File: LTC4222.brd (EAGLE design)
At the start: 160 x 100 mm, 24 parts

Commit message: Forgot to save the first time
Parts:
- added U$3, U$4: 74HC1G86GW-Q100H, Baja_Parts_Lib:SOT65P212X110-5M
- added U$5: SN74HC74QPWRQ1, Baja_Parts_Lib:SOP65P640X120-14M
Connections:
- new net N$1: U$3.2, U$3.4, U$5.2
- new net N$2: U$4.2, U$4.4, U$5.12
- new net N$3: U$12.17, U$5.9
- new net N$4: U$12.24, U$5.5
- net GND: now also U$3.3, U$4.3, U$5.7

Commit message: LTC4222 Schematic Design V2
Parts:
- removed U$1, U$2: TNPW060310K0BEEN, Baja_Parts_Lib:AT0603
- removed U$12: LTC4222, Baja_Parts_Lib:QFN50P500X500X75-33T345M
- removed U$13: AT0603DRD071K82L, Baja_Parts_Lib:RESC1608X45M
- removed U$14: TNPW0603392RBEEA, Baja_Parts_Lib:AT0603
- removed U$15: TNPW0603953RBEEA, Baja_Parts_Lib:AT0603
- removed U$16: CGA3E1X7R1V105K080AE, Baja_Parts_Lib:CAPC1608X80M
- removed U$17: CGA2B3X7R1E683K050BB, Baja_Parts_Lib:CAPC1005X50M
- removed U$18: CGA3E2X7R1H104K080AE, Baja_Parts_Lib:CAPC1608X80M
- removed U$19, U$30: WSL0603R0180FEA, Baja_Parts_Lib:RESC1507X40M
- removed U$20, U$31: PMV15ENEAR, Baja_Parts_Lib:SOT95P230X110-3M
- removed U$21, U$32: TNPW060310R0BEEN, Baja_Parts_Lib:AT0603
- removed U$22: 67997-100HLF, Baja_Parts_Lib:HDRV2W64P254_2X1_241X508X838B
- removed U$23: CGA2B3X7R1V223K050BB, Baja_Parts_Lib:CAPC1005X50M
- removed U$24, U$33: MCT0603PD4991DP500, Baja_Parts_Lib:RESC1508X47M
- removed U$25, U$34: TNPW06033K57BEEA, Baja_Parts_Lib:AT0603
- removed U$27: TNPW060334K0BEEA, Baja_Parts_Lib:AT0603
- removed U$28: TNPW06031K02BEEA, Baja_Parts_Lib:AT0603
- removed U$29: AT0603DRD073K4L, Baja_Parts_Lib:RESC1608X45M
- added C1, C2, C5: CGA3E2X7R1H104K080AE, Baja_Parts_Lib:CAPC1608X80M
- added C3: CGA3E1X7R1V105K080AE, Baja_Parts_Lib:CAPC1608X80M
- added C4: CGA2B3X7R1E683K050BB, Baja_Parts_Lib:CAPC1005X50M
- added C6: CGA2B3X7R1V223K050BB, Baja_Parts_Lib:CAPC1005X50M
- added IC1: 67997-100HLF, Baja_Parts_Lib:HDRV2W64P254_2X1_241X508X838B
- added IC2: LTC4222, Baja_Parts_Lib:QFN50P500X500X75-33T345M
- added J1, J2: PMV15ENEAR, Baja_Parts_Lib:SOT95P230X110-3M
- added R1, R12: WSL0603R0180FEA, Baja_Parts_Lib:RESC1507X40M
- added R10: TNPW0603392RBEEA, Baja_Parts_Lib:AT0603
- added R11: TNPW0603953RBEEA, Baja_Parts_Lib:AT0603
- added R13, R5: TNPW060310R0BEEN, Baja_Parts_Lib:AT0603
- added R14, R8: TNPW060310K0BEEN, Baja_Parts_Lib:AT0603
- added R15, R7: TNPW06033K57BEEA, Baja_Parts_Lib:AT0603
- added R16: MCT0603PD4991DP500, Baja_Parts_Lib:RESC1508X47M
- added R2: TNPW060334K0BEEA, Baja_Parts_Lib:AT0603
- added R3: TNPW06031K02BEEA, Baja_Parts_Lib:AT0603
- added R4: AT0603DRD073K4L, Baja_Parts_Lib:RESC1608X45M
- added R6: TNPW040210K2BEED, Baja_Parts_Lib:RESC1005X35M
- added R9: AT0603DRD071K82L, Baja_Parts_Lib:RESC1608X45M
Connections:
- removed net N$29: U$12.2, U$12.3, U$12.7, U$18.2
- removed net N$30: U$12.11, U$13.1, U$19.2
- removed net N$31: U$20.1, U$21.1, U$22.1
- removed net N$32: U$12.13, U$21.2
- removed net N$33: U$22.2, U$23.2
- removed net N$34: U$12.14, U$2.1, U$20.2, U$23.1, U$24.1
- removed net N$35: U$12.15, U$24.2, U$25.1
- removed net N$36: U$12.32, U$28.2, U$29.1
- removed net N$37: U$12.16, U$2.2
- removed net N$38: U$12.31, U$27.2, U$28.1
- removed net N$39: U$12.30, U$27.1, U$30.1
- removed net N$40: U$12.29, U$30.2, U$31.2
- removed net N$41: U$31.1, U$32.1
- removed net N$42: U$12.28, U$32.2
- removed net N$43: U$1.1, U$12.27, U$31.3, U$33.1
- removed net N$44: U$1.2, U$12.25
- removed net N$45: U$12.26, U$33.2, U$34.1
- new net N$10: C2.2, IC2.2, IC2.3
- new net N$11: IC2.28, R5.1
- new net N$12: IC2.27, J1.2, R6.2, R8.2
- new net N$13: IC2.26, R6.1, R7.2
- new net N$14: IC2.25, R8.1
- new net N$15: C4.2, IC2.8
- new net N$16: C3.2, IC2.1
- new net N$17: C3.1, C4.1
- new net N$18: IC2.13, R13.2
- new net N$19: IC2.9, R10.2, R11.1
- new net N$20: IC2.12, J2.3, R12.2
- new net N$21: IC2.11, R12.1, R9.1
- new net N$22: IC1.1, J2.1, R13.1
- new net N$23: C6.2, IC2.14, J2.2, R14.1, R16.1
- new net N$5: U$4.4, U$5.12
- new net N$6: IC2.29, J1.3, R1.2
- new net N$7: IC2.32, R3.1, R4.1
- new net N$8: C1.2, IC2.31, R2.1, R3.2
- new net N$9: R5.2
- net GND: now also C1.1, C2.1, C5.1, IC2.4, R11.2, R4.2, R7.1; no longer U$12.4, U$15.2, U$16.1, U$17.1, U$18.1, U$25.2, U$29.2, U$34.2
- net N$1: no longer U$3.2
- net N$2: now also IC2.30, R1.1, R2.2; no longer U$4.2, U$4.4, U$5.12
- net N$24: now also C6.1, IC1.2; no longer U$12.10, U$13.2, U$14.1
- net N$25: now also IC2.15, R15.1, R16.2; no longer U$12.9, U$14.2, U$15.1
- net N$26: now also IC2.16, R14.2; no longer U$12.8, U$16.2
- net N$27: now also C5.2, IC2.10, R10.1, R9.2; no longer U$12.1, U$17.2
- net N$28: now also R15.2; no longer U$12.12, U$19.1, U$20.3
- net N$3: now also IC2.17, U$4.1; no longer U$12.17
- net N$4: now also IC2.24, U$3.2; no longer U$12.24

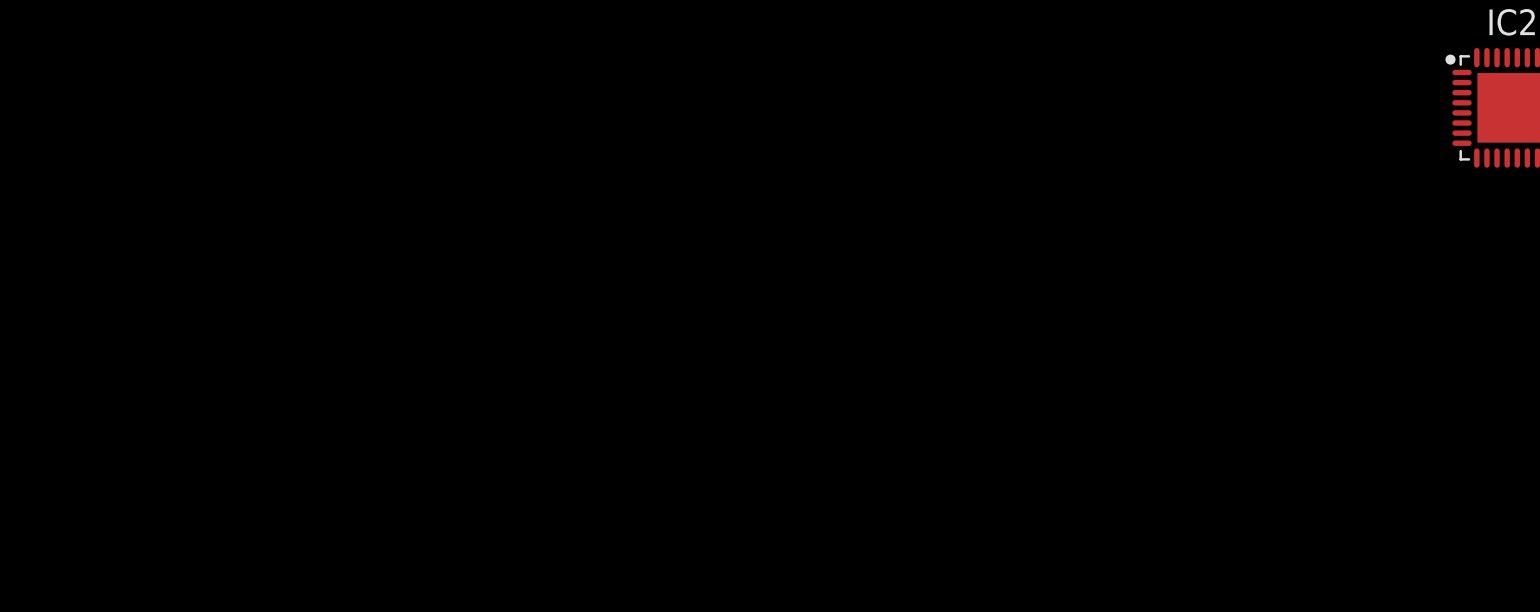
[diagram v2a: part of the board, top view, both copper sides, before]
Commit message: Polished LTC4222 schematic and added test points. Started on pin heads
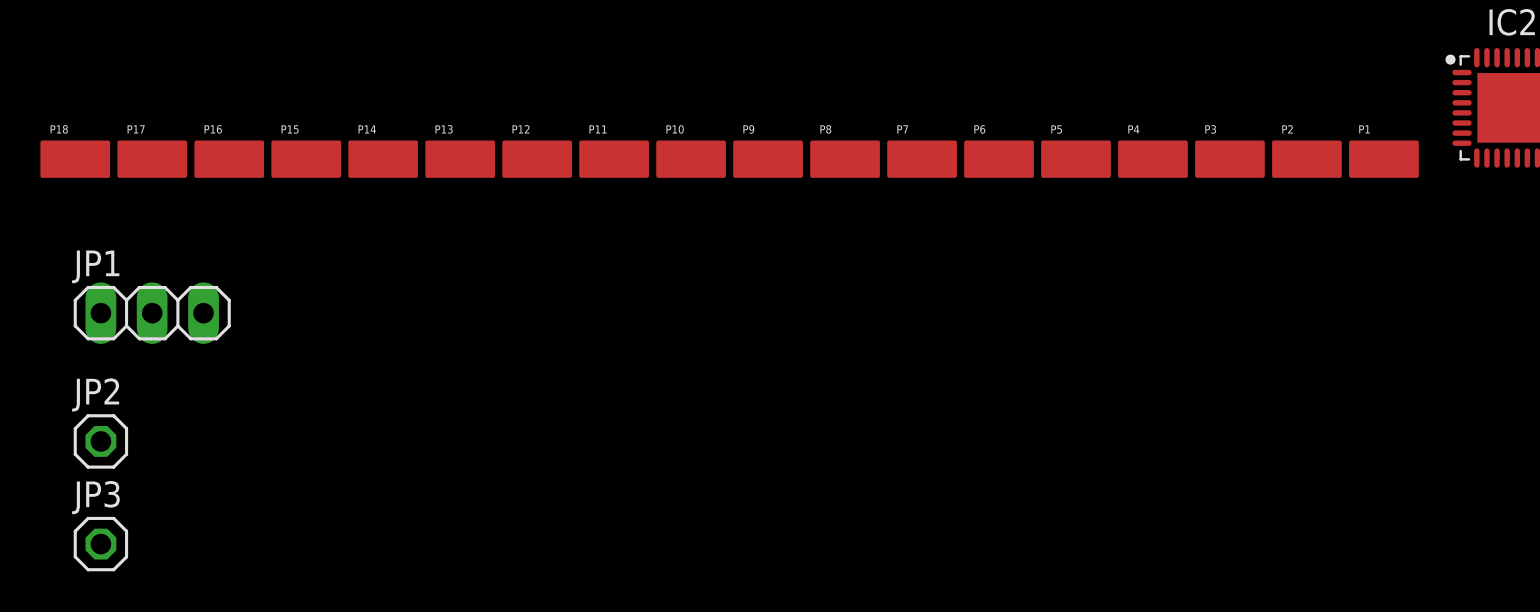
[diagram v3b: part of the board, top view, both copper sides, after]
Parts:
- added JP1: (no value), pinhead:1X03
- added JP2, JP3: (no value), pinhead:1X01
- added P1, P10, P11, P12, P13, P14, P15, P16, P17, P18, P2, P3, P4, P5, P6, P7, P8, P9: S1751-46R, Baja_Parts_Lib:S1751-46R
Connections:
- new net N$29: IC2.26, P7.1, R6.1, R7.2
- new net N$30: IC2.6, JP1.2
- new net N$31: IC2.5, JP1.3
- net N$11: now also P5.1
- net N$12: now also P6.1
- net N$13: now also IC2.7, JP1.1; no longer IC2.26, R6.1, R7.2
- net N$14: now also P8.1
- net N$18: now also P14.1
- net N$19: now also P18.1
- net N$2: now also JP2.1, P2.1
- net N$20: now also P15.1
- net N$21: now also JP3.1, P16.1
- net N$23: now also P13.1
- net N$25: now also P12.1
- net N$26: now also P11.1
- net N$27: now also P17.1
- net N$3: now also P10.1
- net N$4: now also P9.1
- net N$6: now also P4.1
- net N$7: now also P3.1
- net N$8: now also P1.1

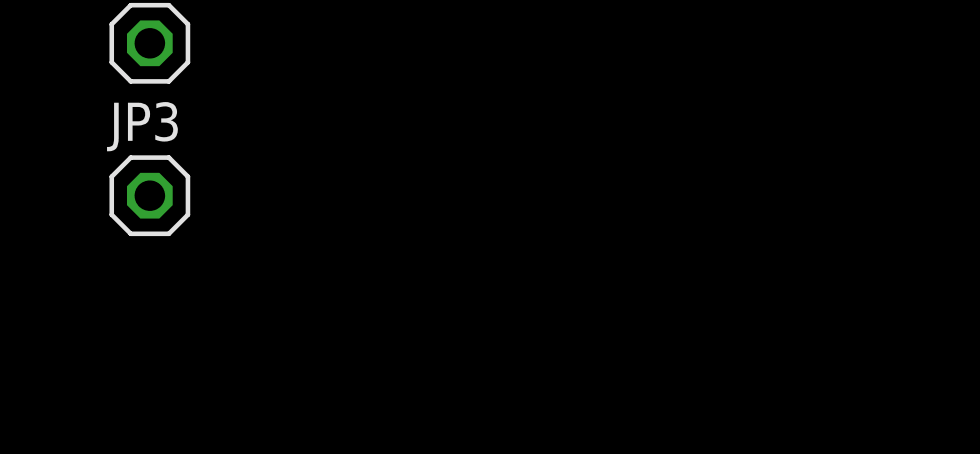
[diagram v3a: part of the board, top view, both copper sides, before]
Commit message: LTC4222 V3; Finished up the headers; Need to source LEDs and LED resistors; Final step = MUX: Check up with Forrest about LDO after final step
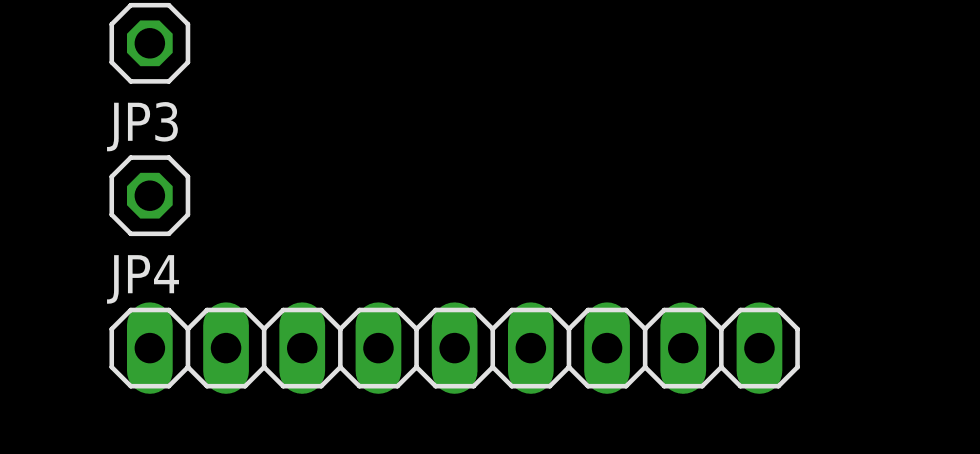
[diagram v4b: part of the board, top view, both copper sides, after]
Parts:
- added JP4: (no value), pinhead:1X09
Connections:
- new net ADIN1: IC2.23, JP4.1
- new net ADIN2: IC2.18, JP4.4
- new net ALERT: IC2.21, JP4.3
- new net A_OR_GATE#2: JP4.7, U$4.2
- new net B_OR_GATE#1: JP4.5, U$3.1
- new net ON: IC2.22, JP4.2
- new net VCC_DFF: JP4.9, U$5.14
- new net VCC_OR_GATE#1: JP4.6, U$3.5
- new net VCC_OR_GATE#2: JP4.8, U$4.5
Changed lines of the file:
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@@
 <attribute name="VALUE" x="-312.42" y="-196.215" size="1.27" layer="27"/>
+</element>
+<element name="JP4" library="pinhead" library_urn="urn:adsk.eagle:library:325" package="1X09" package3d_urn="urn:adsk.eagle:package:22483/2" value="" x="-300.99" y="-198.12" smashed="yes">
+<attribute name="NAME" x="-312.4962" y="-196.2912" size="1.27" layer="25" ratio="10"/>
+<attribute name="POPULARITY" value="13" x="-300.99" y="-198.12" size="1.778" layer="27" display="off"/>
+<attribute name="VALUE" x="-312.42" y="-201.295" size="1.27" layer="27"/>
 </element>
 </elements>
@@
 <wire x1="-243.7846" y1="-171.7" x2="-306.07" y2="-181.61" width="0" layer="19" extent="1-1"/>
 </signal>
+<signal name="A_OR_GATE#2">
+<contactref element="JP4" pad="7"/>
+<contactref element="U$4" pad="2"/>
+<wire x1="-72.1445" y1="-12.7" x2="-295.91" y2="-198.12" width="0" layer="19" extent="1-1"/>
+</signal>
+<signal name="VCC_DFF">
+<contactref element="JP4" pad="9"/>
+<contactref element="U$5" pad="14"/>
+<wire x1="-82.1683" y1="-8.21" x2="-290.83" y2="-198.12" width="0" layer="19" extent="1-1"/>
+</signal>
+<signal name="VCC_OR_GATE#1">
+<contactref element="U$3" pad="5"/>
+<contactref element="JP4" pad="6"/>
+<wire x1="-65.0155" y1="-4.43" x2="-298.45" y2="-198.12" width="0" layer="19" extent="1-1"/>
+</signal>
+<signal name="B_OR_GATE#1">
+<contactref element="U$3" pad="1"/>
+<contactref element="JP4" pad="5"/>
+<wire x1="-67.0645" y1="-4.43" x2="-300.99" y2="-198.12" width="0" layer="19" extent="1-1"/>
+</signal>
+<signal name="VCC_OR_GATE#2">
+<contactref element="U$4" pad="5"/>
+<contactref element="JP4" pad="8"/>
+<wire x1="-70.0955" y1="-12.05" x2="-293.37" y2="-198.12" width="0" layer="19" extent="1-1"/>
+</signal>
+<signal name="ADIN2">
+<contactref element="JP4" pad="4"/>
+<contactref element="IC2" pad="18"/>
+<wire x1="-238.8154" y1="-172.7" x2="-303.53" y2="-198.12" width="0" layer="19" extent="1-1"/>
+</signal>
+<signal name="ALERT">
+<contactref element="IC2" pad="21"/>
+<contactref element="JP4" pad="3"/>
+<wire x1="-238.8154" y1="-171.2" x2="-306.07" y2="-198.12" width="0" layer="19" extent="1-1"/>
+</signal>
+<signal name="ON">
+<contactref element="IC2" pad="22"/>
+<contactref element="JP4" pad="2"/>
+<wire x1="-238.8154" y1="-170.7" x2="-308.61" y2="-198.12" width="0" layer="19" extent="1-1"/>
+</signal>
+<signal name="ADIN1">
+<contactref element="JP4" pad="1"/>
+<contactref element="IC2" pad="23"/>
+<wire x1="-311.15" y1="-198.12" x2="-238.8154" y2="-170.2" width="0" layer="19" extent="1-1"/>
+</signal>
 </signals>

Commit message: Began working on the PCB schematic and actually saving on git
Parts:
- moved JP2 424.5 mm to (5.08, 95.2)
- moved P2 379.0 mm to (19.1, 91.4)
- moved IC2 371.9 mm to (47.0, 63.5)
- moved R16 370.7 mm to (76.2, 40.6)
- moved JP4 370.0 mm to (-36.8, 61.0)
- moved P3 359.4 mm to (6.35, 72.4)
- moved JP3 359.0 mm to (-73.7, 76.2)
- moved JP1 357.5 mm to (-61.0, 76.2)
- moved R15 355.4 mm to (62.2, 48.3)
- moved P1 353.1 mm to (-5.08, 82.5)
- moved P15 349.7 mm to (-64.8, 83.8)
- moved P16 349.7 mm to (-68.6, 83.8)
- moved P17 349.7 mm to (-72.4, 83.8)
- moved P18 349.7 mm to (-76.2, 83.8)
- moved P10 349.7 mm to (-45.7, 83.8)
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
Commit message: Test message V2
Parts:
- removed JP4: (no value), pinhead:1X09
- removed P10, P9: S1751-46R, Baja_Parts_Lib:S1751-46R
- removed U$3, U$4: 74HC1G86GW-Q100H, Baja_Parts_Lib:SOT65P212X110-5M
- removed U$5: SN74HC74QPWRQ1, Baja_Parts_Lib:SOP65P640X120-14M
- moved P13 115.1 mm to (35.1, 15.0), turned to 90 degrees
- moved P11 114.4 mm to (48.0, 24.1)
- moved P12 114.2 mm to (38.5, 16.0), turned to 90 degrees
- moved P18 112.8 mm to (17.7, 21.2)
- moved P16 112.3 mm to (18.8, 13.2), turned to 90 degrees
- moved P17 111.7 mm to (12.6, 11.3)
- moved P15 111.6 mm to (23.9, 16.0), turned to 90 degrees
- moved P14 111.6 mm to (28.3, 16.9), turned to 90 degrees
- moved JP3 106.8 mm to (5.33, 4.32)
- moved P8 96.4 mm to (43.4, 32.4)
- moved JP1 84.7 mm to (9.53, 29.2), turned to 90 degrees
- moved P7 84.6 mm to (34.8, 34.9), turned to 90 degrees
- moved P6 75.8 mm to (38.6, 52.7)
- moved P5 74.0 mm to (33.1, 40.3), turned to 90 degrees
- moved P4 64.3 mm to (28.8, 45.6), turned to 90 degrees
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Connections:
- removed net A_OR_GATE#2: JP4.7, U$4.2
- removed net B_OR_GATE#1: JP4.5, U$3.1
- removed net N$1 (its old number): U$3.4, U$5.2
- removed net N$3: IC2.17, P10.1, U$4.1, U$5.9
- removed net N$4: IC2.24, P9.1, U$3.2, U$5.5
- removed net N$5: U$4.4, U$5.12
- removed net VCC_DFF: JP4.9, U$5.14
- removed net VCC_OR_GATE#1: JP4.6, U$3.5
- removed net VCC_OR_GATE#2: JP4.8, U$4.5
- net ADIN1: no longer JP4.1
- net ADIN2: no longer JP4.4
- net ALERT: no longer JP4.3
- net GND: no longer U$3.3, U$4.3, U$5.7
- net ON: no longer JP4.2
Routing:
- net N$12: track 0.00 -> 47.9 mm
- net N$21: track 0.00 -> 43.2 mm
- net N$23: track 0.00 -> 38.4 mm
- net N$26: track 0.00 -> 38.3 mm
- net N$2: track 0.00 -> 36.9 mm
- net N$27: track 0.00 -> 36.8 mm
- net N$19: track 0.00 -> 35.4 mm
- net N$25: track 0.00 -> 32.7 mm
- net N$8: track 0.00 -> 31.6 mm
- net N$20: track 0.00 -> 26.5 mm
- net N$29: track 0.00 -> 26.4 mm
- net N$16: track 0.00 -> 24.3 mm
- net N$7: track 0.00 -> 24.2 mm
- net N$6: track 0.00 -> 24.1 mm
- net N$14: track 0.00 -> 23.6 mm
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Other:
- board size 160 x 100 mm -> 55.9 x 59.4 mm

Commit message: Small alterations
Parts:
- moved C3 5.25 mm to (8.26, 35.3)
- moved C4 4.36 mm to (7.75, 23.9)
- moved R7 4.02 mm to (41.0, 37.6)
- moved R8 3.75 mm to (45.1, 44.8)
- moved P5 3.61 mm to (35.4, 43.1)
- moved R5 3.51 mm to (35.8, 47.1)
- moved R11 3.31 mm to (10.9, 21.3)
- moved P6 2.54 mm to (41.1, 52.7)
- moved R6 2.32 mm to (41.0, 45.1)
- moved JP1 2.16 mm to (11.7, 29.2)
- moved J2 1.65 mm to (27.8, 4.45), turned to 180 degrees
- moved R9 1.65 mm to (12.7, 7.87)
- moved JP3 1.61 mm to (5.84, 5.84)
- moved R12 1.53 mm to (21.6, 5.84)
- moved J1 1.40 mm to (33.0, 52.1)
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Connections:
- net N$1: now also J1.1
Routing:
- net N$23: track 38.4 -> 49.6 mm, vias 0 -> 2
- net N$19: track 35.4 -> 29.1 mm
- net N$16: track 24.3 -> 18.7 mm
- net N$15: track 22.1 -> 17.6 mm
- net N$22: track 10.5 -> 14.8 mm
- net N$1: track 0.00 -> 3.97 mm
- net N$14: track 23.6 -> 27.6 mm
- net N$17: track 15.8 -> 12.4 mm
- net N$20: track 26.5 -> 23.4 mm
- net N$21: track 43.2 -> 41.0 mm
- net N$31: track 17.6 -> 15.5 mm
- net N$30: track 16.8 -> 14.6 mm
- net N$13: track 15.9 -> 13.8 mm
- net N$12: track 47.9 -> 49.8 mm
- net N$27: track 36.8 -> 35.2 mm
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
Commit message: PCB Design V1
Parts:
- moved P12 2.01 mm to (40.1, 17.1)
- moved P8 1.40 mm to (44.8, 32.5)
- moved R3 1.40 mm to (18.5, 44.5)
- moved R11 1.14 mm to (12.1, 21.3)
- moved P2 1.02 mm to (22.1, 52.6)
- moved P4 1.02 mm to (29.8, 45.6)
- moved JP2 0.85 mm to (11.3, 52.5)
- moved C4 0.74 mm to (7.37, 24.5)
- moved C2 0.65 mm to (17.0, 30.4)
- moved R15 0.38 mm to (43.6, 18.0)
- moved R5 0.38 mm to (35.4, 47.1)
- moved P18 0.36 mm to (17.9, 21.0)
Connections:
- removed net N$17: C3.1, C4.1
- removed net N$28: R15.2
- net GND: now also C3.1, C4.1, R15.2
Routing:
- net N$17: track 12.4 -> 0.00 mm
- net N$19: track 29.1 -> 23.7 mm
- net N$2: track 36.9 -> 41.7 mm
- net N$12: track 49.8 -> 45.5 mm
- net N$20: track 23.4 -> 27.6 mm
- net N$10: track 9.43 -> 13.3 mm
- net N$23: track 49.6 -> 52.5 mm
- net N$22: track 14.8 -> 12.1 mm
- net N$11: track 19.4 -> 21.8 mm
- net N$7: track 24.2 -> 22.4 mm
- net N$8: track 31.8 -> 33.1 mm
- net N$24: track 6.76 -> 8.00 mm
- net N$14: track 27.6 -> 28.4 mm
- net N$6: track 25.4 -> 26.2 mm
- net GND: track 8.29 -> 8.98 mm, vias 1 -> 6
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- added copper zone on layer 1, net GND
- added copper zone on layer 16, net GND
